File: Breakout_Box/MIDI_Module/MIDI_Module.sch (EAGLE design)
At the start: 71 parts, among them T1 MMBT2222LT1G, T2 MMBT2222LT1G, U1 TLV6004, U2 TLV6004, U3 MIC5205-5.0YM5-TR, U4 MIC5205-3.3YM5-TR

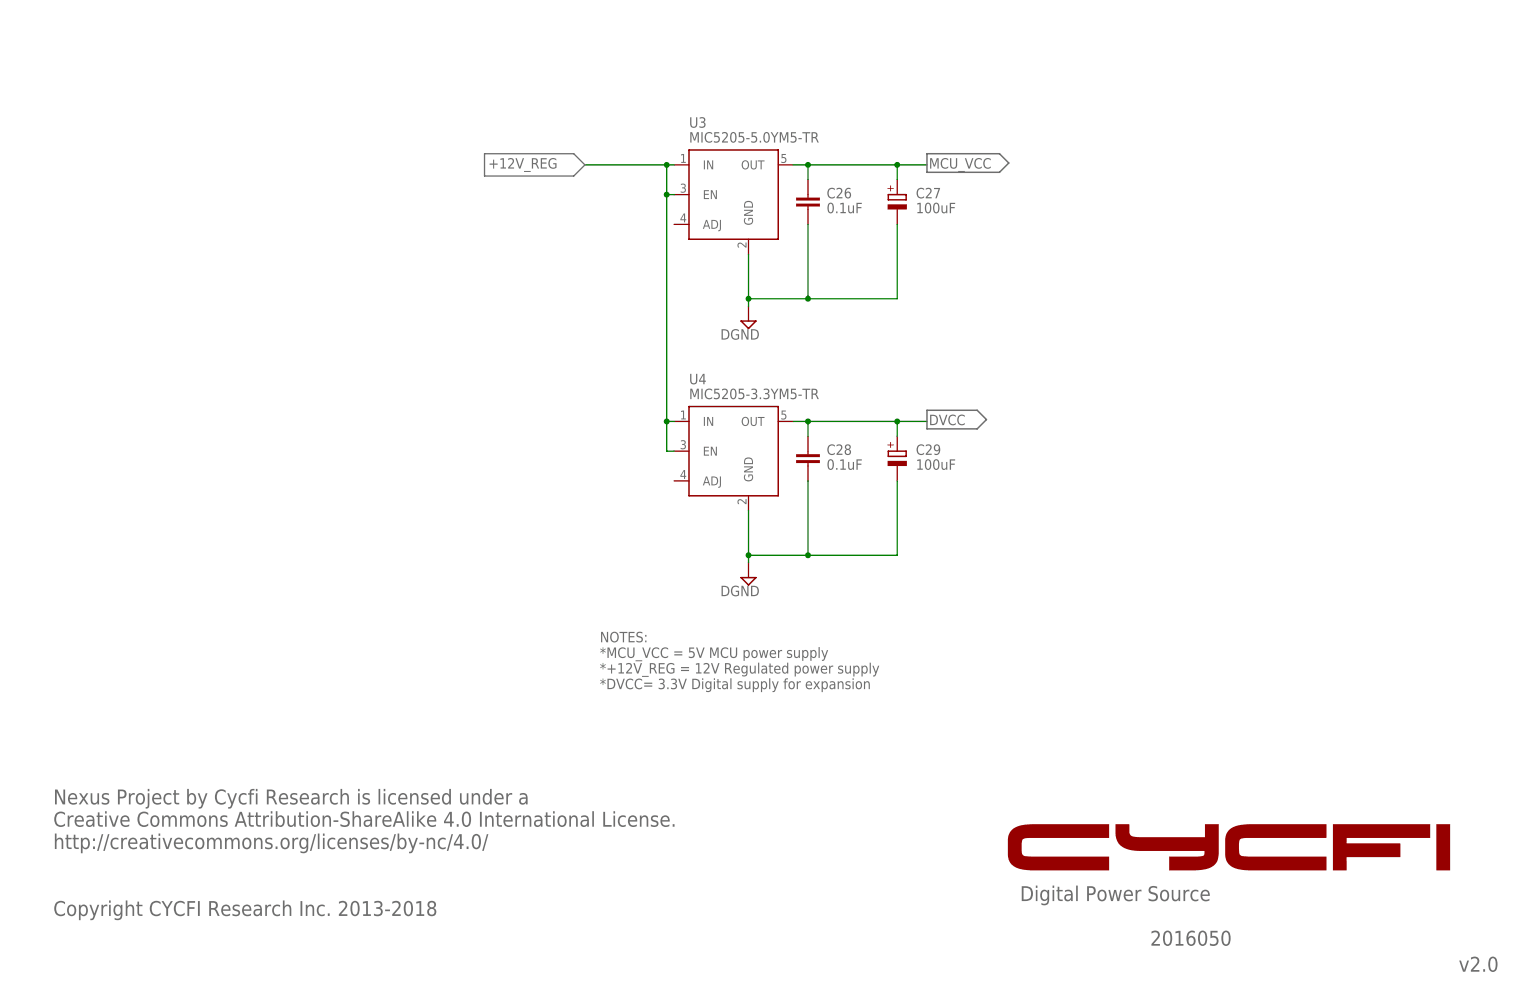
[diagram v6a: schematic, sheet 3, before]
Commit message: Upload MIDI board for v2.2
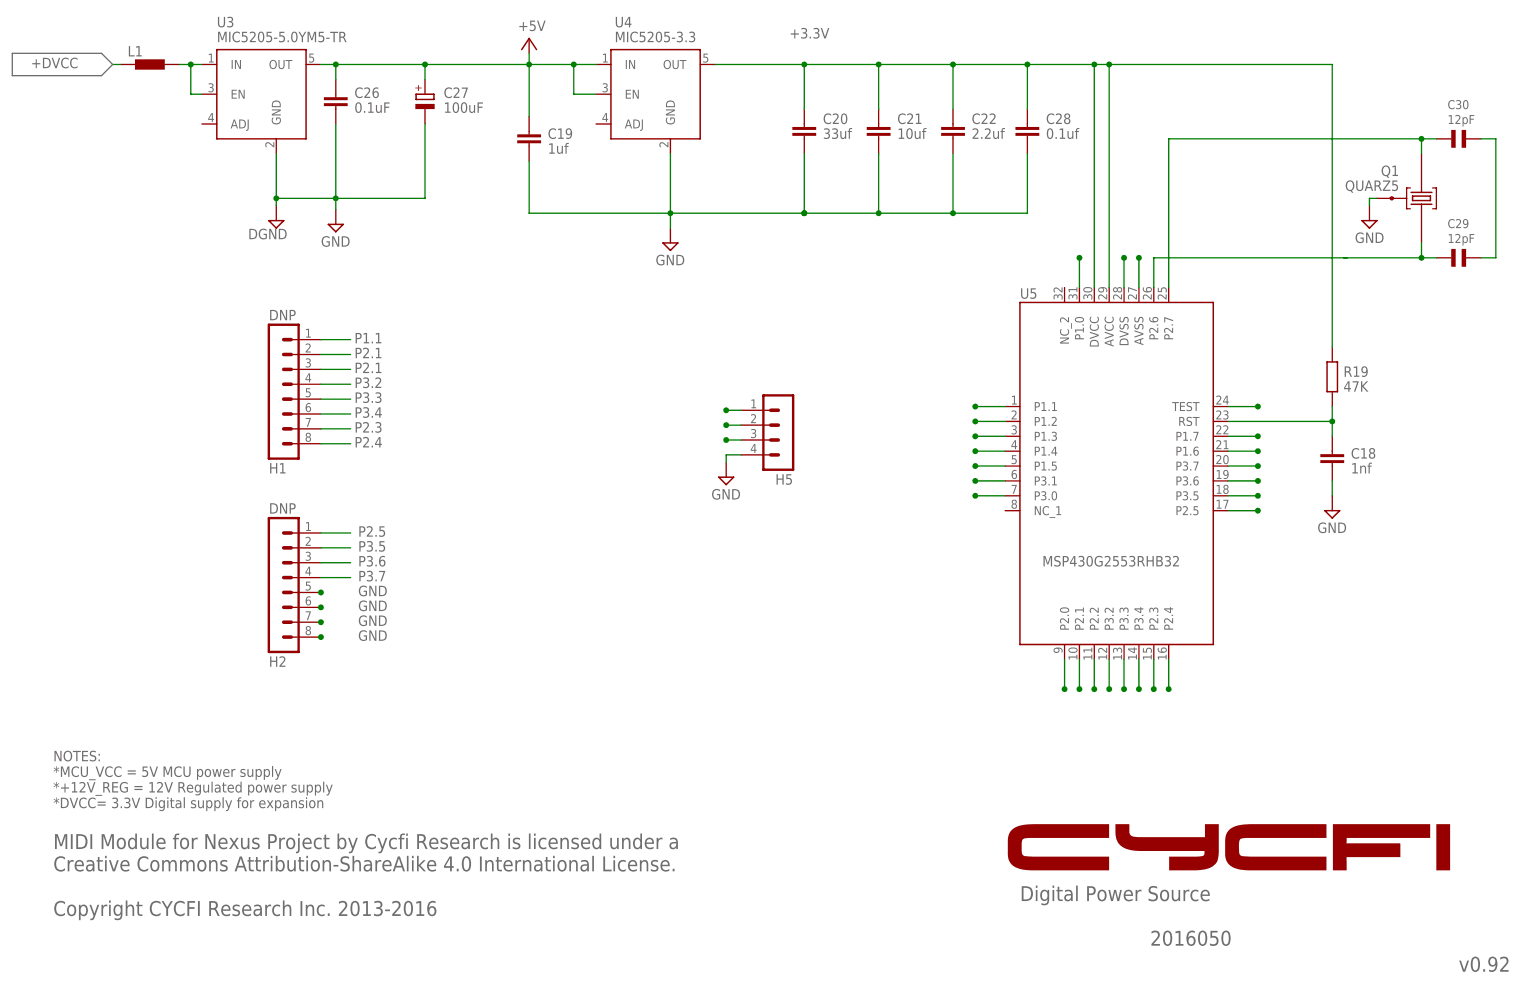
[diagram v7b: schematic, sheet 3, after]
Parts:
- added C18: 1nf, resistor:C-EUC0603
- added C19: 1uf, resistor:C-EUC0805
- added C20: 33uf, resistor:C-EUC0805
- added C21: 10uf, resistor:C-EUC0805
- added C22: 2.2uf, resistor:C-EUC0805
- added C30: 12pF, ssmd:C_SMD0603
- added H5: (no value), con-lstb:MA04-1
- added L1: BLM15HB121SN1, inductors:BLM15HB121SN1
- added Q1: QUARZ5, sMSP430:QUARZ5
- added R19: 47K, resistor:R-EU_R0402
- added U5: MSP430G2553RHB32, CYCFI_IC:MSP430G2553RHB32
- C28: value 0.1uF -> 0.1uf
- C29: value 100uF -> 12pF; device resistor:CPOL-EU153CLV-0505 -> ssmd:C_SMD0603
- H1, H2: value 14PIN-TH-2.54MM -> DNP; device CYCFI_Con:14PIN-TH-2.54MM -> con-lstb:MA08-1
- H3, H4: value (none) -> DNP
- R10, R52, R53, R54, R6, R8: value 520 -> 5.1k
- R11, R4, R55, R56, R57, R7, R9: value 1K -> 10k
- R5: value 520 -> 10k
- T1, T2: value MMBT2222LT1G -> 2N2222
- U1, U2: value TLV6004 -> LMV324; device CYCFI_semicon:TLV6004 -> CYCFI_semicon:LMV324
- U4: value MIC5205-3.3YM5-TR -> MIC5205-3.3
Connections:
- removed net +12V_REG: H9.1, H9.2, H9.3, H9.4, U3.EN, U3.IN, U4.EN, U4.IN
- removed net CH10A: C25.1, H2.12, R54.2, R57.1
- removed net CH11A: C5.1, H1.5, R10.2, R11.1
- removed net CH12A: C13.1, H1.6, R8.2, R9.1
- removed net CH13A: C12.1, H1.7, R6.2, R7.1
- removed net CH14A: C23.1, H2.8, R52.2, R55.1
- removed net CH15A: C24.1, H2.9, R53.2, R56.1
- removed net CH9D: C4.1, H1.10, R4.1, R5.2
- removed net DVCC: C28.1, C29.+, H4.2, H4.4, H4.6, H4.8, U4.OUT
- removed net MCU_VCC: C1.1, C2.1, C26.1, C27.+, C3.1, C6.1, C7.1, C8.1, H2.13, H2.14, H3.2, H3.4, H3.6, H3.8, R1.2, R75.2, U1P1.V+, U2P1.V+, U3.OUT
- removed net MIDI_OUT: H1.4, R74.1, TP_SER.TP
- removed net N$6: H1.9
- removed net P2.2: H1.12
- removed net P2.6: H2.11
- removed net P2.7: H2.10
- removed net P3.1: H1.8
- new net !RST: C18.1, R19.2, U5.RST
- new net !RST1: H5.2
- new net +3.3V: C20.1, C21.1, C22.1, C28.1, H4.2, H4.4, H4.6, H4.8, R19.1, U4.OUT, U5.AVCC, U5.DVCC
- new net +5V: C1.1, C19.1, C2.1, C26.1, C27.+, C3.1, C6.1, C7.1, C8.1, H3.2, H3.4, H3.6, H3.8, R1.2, R75.2, U1P1.V+, U2P1.V+, U3.OUT, U4.EN, U4.IN
- new net +DVCC: H9.1, H9.2, H9.3, H9.4, L1.1
- new net DVCC(3.3V): H5.3
- new net GND: C18.2, C19.2, C20.2, C21.2, C22.2, C26.2, C27.-, C28.2, C29.1, C30.1, H2.5, H2.6, H2.7, H2.8, H5.4, Q1.0, U3.GND, U4.GND, U5.AVSS, U5.DVSS
- new net N$12: L1.2, U3.EN, U3.IN
- new net P1.0: C25.1, R54.2, R57.1, U5.P1.0
- new net P1.2: R74.1, TP_SER.TP, U5.P1.1
- new net P1.3: C5.1, R10.2, R11.1, U5.P1.2
- new net P1.4: C13.1, R8.2, R9.1, U5.P1.3
- new net P1.5: C12.1, R6.2, R7.1, U5.P1.4
- new net P1.6: C23.1, R52.2, R55.1, U5.P1.5
- new net P1.7: C24.1, R53.2, R56.1, U5.P1.6
- new net P1.8: U5.P1.7
- new net P2.0: C4.1, R4.1, R5.2, U5.P2.0
- new net P2.10: U5.P2.3
- new net P2.11: U5.P2.4
- new net P2.12: U5.P2.5
- new net P2.13: C29.2, Q1.1, U5.P2.6
- new net P2.14: C30.2, Q1.2, U5.P2.7
- new net P2.8: U5.P2.1
- new net P2.9: U5.P2.2
- new net P3.10: U5.P3.7
- new net P3.11: U5.P3.6
- new net P3.12: U5.P3.5
- new net P3.13: U5.P3.2
- new net P3.14: U5.P3.3
- new net P3.15: U5.P3.4
- new net P3.8: U5.P3.1
- new net P3.9: U5.P3.0
- new net TEST: U5.TEST
- new net TEST1: H5.1
- net DGND: no longer C26.2, C27.-, C28.2, C29.-, H1.1, H1.2, U3.GND, U4.GND
- net P1.1: now also H1.1; no longer H1.3
- net P2.1: now also H1.2, H1.3; no longer H1.11
- net P2.3: now also H1.7; no longer H2.2
- net P2.4: now also H1.8; no longer H2.3
- net P2.5: now also H2.1; no longer H2.4
- net P3.2: now also H1.4; no longer H1.13
- net P3.3: now also H1.5; no longer H1.14
- net P3.4: now also H1.6; no longer H2.1
- net P3.5: now also H2.2; no longer H2.5
- net P3.6: now also H2.3; no longer H2.6
- net P3.7: now also H2.4; no longer H2.7
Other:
- note added: "!RST"
- note added: "DVCC"
- note added: "GND"
- note added: "MIDI Module for Nexus Project by Cycfi Research is licensed under a Creative Commons Attribution-ShareAlike 4.0 International License. Copyright CYCFI Research Inc. 2013-2016"
- note added: "PROG PINS"
- note added: "TEST"
- note added: "v0.9"
- note added: "v0.92"
- note removed: "DVCC 3.3V"
- note removed: "MCU_VCC 5V"
- note removed: "Nexus Project by Cycfi Research is licensed under a Creative Commons Attribution-ShareAlike 4.0 International License. http://creativecommons.org/licenses/by-nc/4.0/ Copyright CYCFI Research Inc. 2013-2018"
- note removed: "Note: *TP_XX = Test Point"
- note removed: "v2.0"
- moved on the sheet: C26, C27, C28, U3, U4
